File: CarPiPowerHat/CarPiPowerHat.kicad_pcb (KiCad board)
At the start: 4 copper layers, 96 x 85 mm, 119 parts, among them IC1 AP2331TDSA-7, J1 HDMI_A_1.4, J10 Conn_01x02_Male, J2 1-84953-5, J3 40HAT, J4 Conn_02x03_Counter_Clockwise, J5 USB_A, J6 1-84953-5, J7 HDMI_A_1.4, J8 AudioJack2_Ground, J9 Conn_01x04, Q1 DMMT5401, Q2 DMG2305UX, Q3 DMP3013SFV-7, Q4 DMG2305, U1 AP64501SP-13, U2 CAT24C32, U3 LM3480-5.0, U4 ATtiny45V-10X, U5 PCF85063AT/AAZ, U7 AP2112-3.3K, U8 UDA1334ATS, Y1 X32K768S301

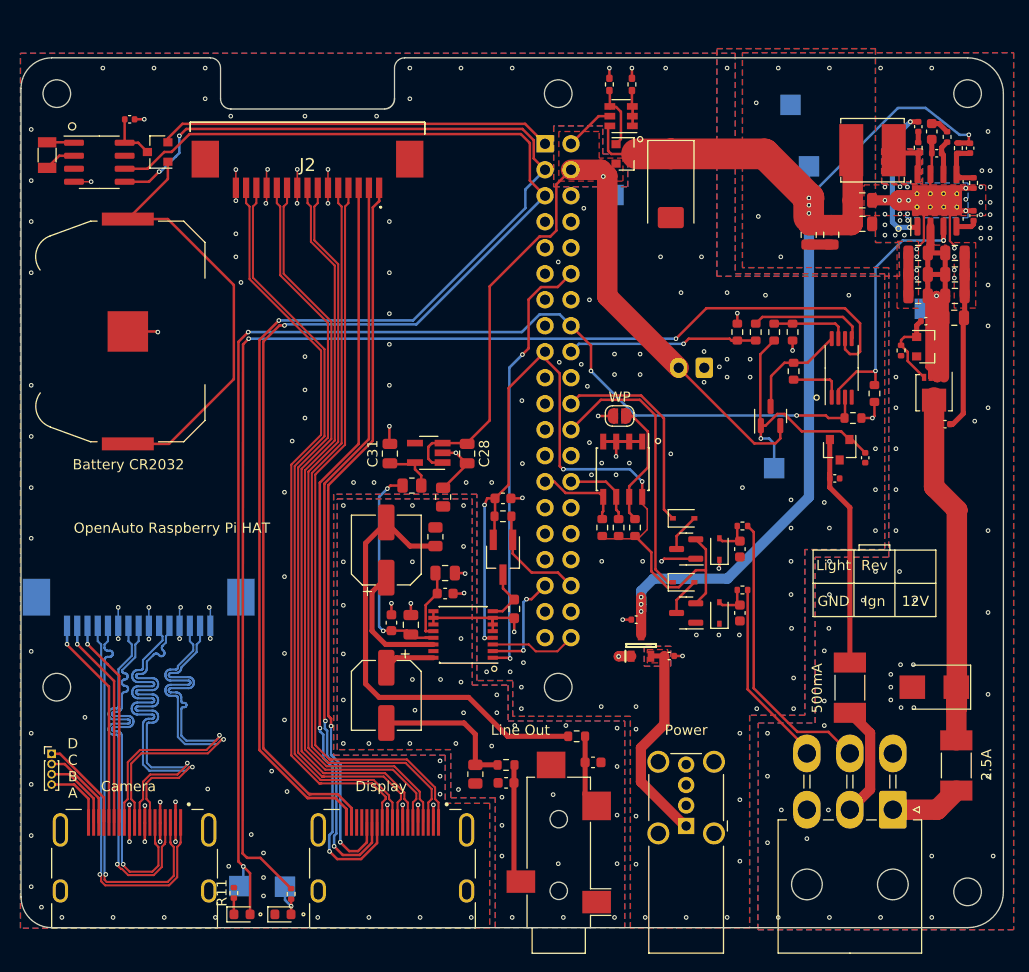
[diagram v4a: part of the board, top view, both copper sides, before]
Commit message: Added part numbers
* Selected parts from lcsc
* Checked footprints
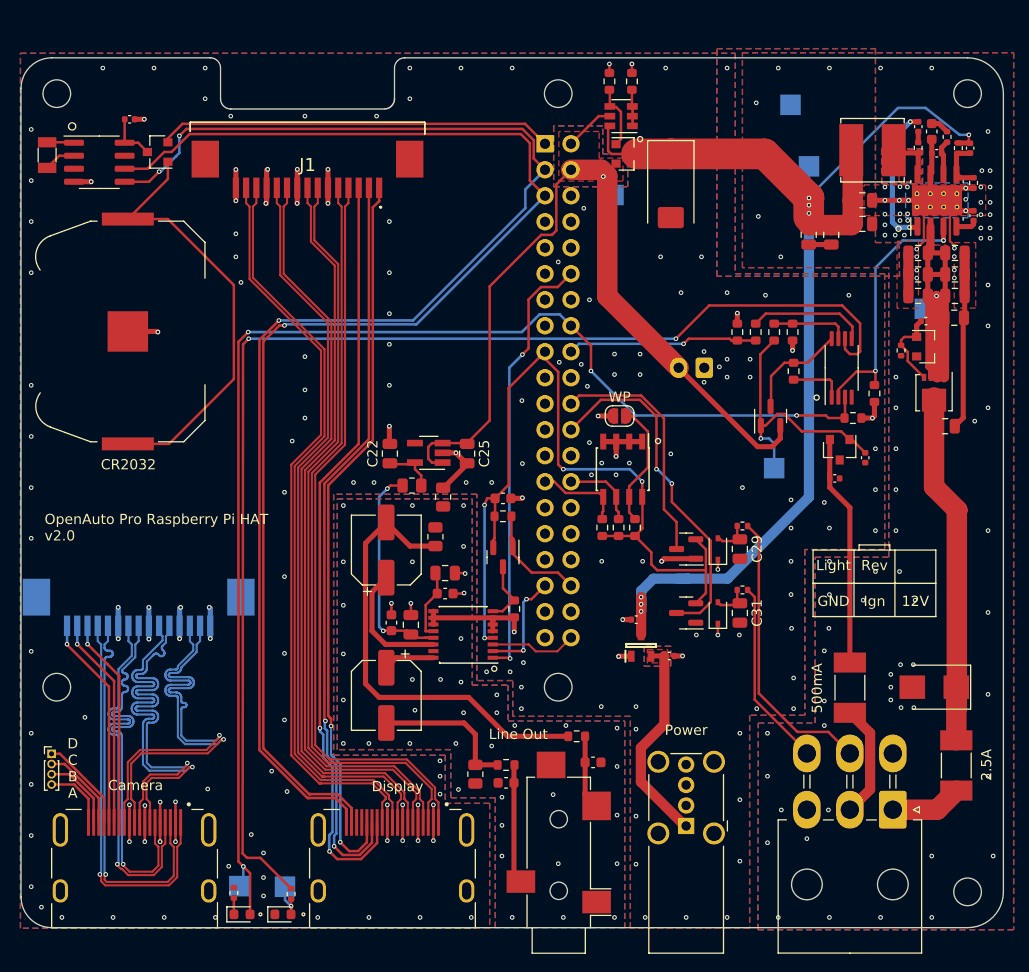
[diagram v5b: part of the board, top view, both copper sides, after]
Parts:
- removed the D10 at (142.8, 82.7)
- removed the D8 at (142.8, 76.5)
- C1: renamed from C24; value 100n -> 100n 16v
- C13: renamed from C9; value 100n -> 100n 16v
- C16: renamed from C8; value 100n -> 100n 16v
- C18: renamed from C10; value 100n -> 100n 16v
- C23: renamed from C25; value 100n -> 100n 16v
- C29: renamed from C22; footprint Capacitor_SMD:C_0603_1608Metric -> Capacitor_SMD:C_0805_2012Metric
- C30: renamed from C21; value 100n -> 100n 16v
- C31: renamed from C23; footprint Capacitor_SMD:C_0603_1608Metric -> Capacitor_SMD:C_0805_2012Metric
- C32: renamed from C20; value 100n -> 100n 16v
- C33: renamed from C4; footprint Capacitor_SMD:C_0402_1005Metric -> Capacitor_SMD:C_0805_2012Metric
- C37: renamed from C26; value 100n -> 100n 16v
- Q2: value DMG2305UX -> DMG2305
- Q3: renamed from Q4; value DMG2305 -> DMG2305; footprint Package_TO_SOT_SMD:SOT-23W_Handsoldering -> Package_TO_SOT_SMD:SOT-23
- R1: renamed from R4; footprint Resistor_SMD:R_0402_1005Metric_Pad0.72x0.64mm_HandSolder -> Resistor_SMD:R_0603_1608Metric
- R16: renamed from R23; footprint Resistor_SMD:R_0603_1608Metric_Pad0.98x0.95mm_HandSolder -> Resistor_SMD:R_0603_1608Metric
- R19: renamed from R21; value 200 -> 220
- R2: renamed from R1; footprint Resistor_SMD:R_0402_1005Metric_Pad0.72x0.64mm_HandSolder -> Resistor_SMD:R_0603_1608Metric
- R21: renamed from R20; value 200 -> 220
- moved R1 0.30 mm to (135.5, 33.8)
- moved R2 0.30 mm to (137.7, 33.8)
- moved C33 0.20 mm to (168.3, 67.5)
- moved D3 0.15 mm to (146.1, 79.5)
- moved D6 0.15 mm to (146.1, 85.7)
- renumbered C3 to C10, C5 to C11, C14 to C12, C2 to C14, C13 to C15, C11 to C17, C7 to C19, C15 to C2, C30 to C20, C33 to C21, C31 to C22, C35 to C24, C28 to C25, C27 to C26, C29 to C27, C32 to C28, C16 to C3, C37 to C35, C17 to C4, C19 to C5, C18 to C6, C6 to C7, C1 to C8, C12 to C9, D15 to D1, D2 to D10, D4 to D2, D7 to D3, D6 to D4, D9 to D5, D11 to D6, D5 to D7, D3 to D8, D1 to D9, F2 to F1, F1 to F2, FB4 to FB2, H3 to H1, H1 to H2, H6 to H3, H2 to H5, H5 to H6, J2 to J1, J6 to J10, J9 to J2, J1 to J3, J8 to J4, J7 to J5, J5 to J6, J4 to J7, J10 to J8, J3 to J9, Q3 to Q4, R9 to R10, R7 to R11, R22 to R13, R8 to R14, R24 to R15, R6 to R17, R3 to R18, R13 to R20, R16 to R22, R11 to R23, R18 to R24, R27 to R26, R26 to R27, R19 to R3, R5 to R4, R28 to R5, R17 to R6, R14 to R7, R15 to R8, R10 to R9, TP3 to TP1, TP1 to TP2, TP2 to TP3, TP5 to TP4, TP4 to TP5, U5 to U1, U4 to U2, U1 to U3, U2 to U4, U7 to U5, U8 to U6, U3 to U7
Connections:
- net /HDMI Connector Display/A renamed /RTC Clock/SDA
- D5 pad 3: Net-(D10-Pad2) -> /Light Input/OUT
- D7 pad 3: Net-(D5-Pad3) -> /Raspberry Pi/BCM25
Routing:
- net GND: track 157.9 -> 165.9 mm, vias 268 -> 272
- net /Light Input/OUT: track 27.4 -> 34.4 mm, vias 0 -> 2
- net Net-(D5-Pad3): track 3.72 -> 0.00 mm
- net Net-(D10-Pad2): track 3.72 -> 0.00 mm
- net /Raspberry Pi/BCM25: track 20.5 -> 23.6 mm
- net /+3.3v: track 122.5 -> 120.8 mm
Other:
- board text added: "CR2032"
- board text added: "OpenAuto Pro Raspberry Pi HAT v2.0"
- board text removed: "Battery CR2032"
- board text removed: "OpenAuto Raspberry Pi HAT"
